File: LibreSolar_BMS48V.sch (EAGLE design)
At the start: 185 parts, among them IC1 BQ76940, Q1 ZXMP10A13F, Q10 DMN2004K, Q11 DMN2004K, Q12 DMN2004K, Q13 DMN2004K, Q14 DMN2004K, Q15 DMN2004K, Q16 DMN2004K, Q17 DMN2004K, Q18 DMN2004K, Q19 DMN2004K, Q2 FDMT80080DC, Q3 FDMT80080DC, Q4 2N7002ET1G, Q5 DMN2004K, Q6 DMN2004K, Q7 DMN2004K, Q8 DMN2004K, Q9 DMN2004K, U1 BQ76200, U2 LMR16006X, U3 ATMEGA328, Y1 8MHz

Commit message: Pinout of extension connector (LSX) changed
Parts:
- C10: value 4.7µ -> 1µ
- C11, C14, C16, C18: MF AVX -> MURATA; MPN 08053C105KAT2A -> GRM188R71E105KA12D; OC_FARNELL 1658877 -> 1735540
- C19: value 470n -> 1µ
- C20, C21: MF WALSIN -> MURATA; MPN 0603B104K500CT -> GRM188R71H103KA01D.; OC_FARNELL 2496834 -> 8819980
- C40: MF AVX -> WALSIN; MPN 08055C104KAT2A -> 0603B104K500CT
- D23, D24, D25, D26, H1, H2, H3, H4, JP4: OC_FARNELL (none) -> unknown
- L1: MF (none) -> COILCRAFT; MPN (none) -> LPS5030-104MLC
- LMX1: device resolut:LIBRE-STANDARD-EXTENSION -> LibreSolar:LIBRE-STD-EXT_SMALL
- Q1: MF (none) -> DIODES INC.; MPN (none) -> ZXMP10A13FTA; OC_FARNELL (none) -> 1843777
- R10: value 5m -> 1m
- R76: MF MULTICOMP -> PANASONIC ELECTRONIC COMPONENTS; MPN MCMR06X1001FTL -> ERJU06F1004V; OC_FARNELL 2073348 -> 2145441
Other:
- note added: "25V"
- note added: "Take resistor with low temperature coefficient and 3W thermal rating, e.g.: Bourns CRE2512-FZ-R001E-3 (75 ppm/K, 3W, 1%)"
- note added: "ToDo: - Mehrere Rsense parallel (package 2512 selbst bei 1 mOhm Widerstand nicht ausreichend für Verlustleistung)"
- note added: "Total gate capacitance of both FETs approx 40nF (see slva729a)"

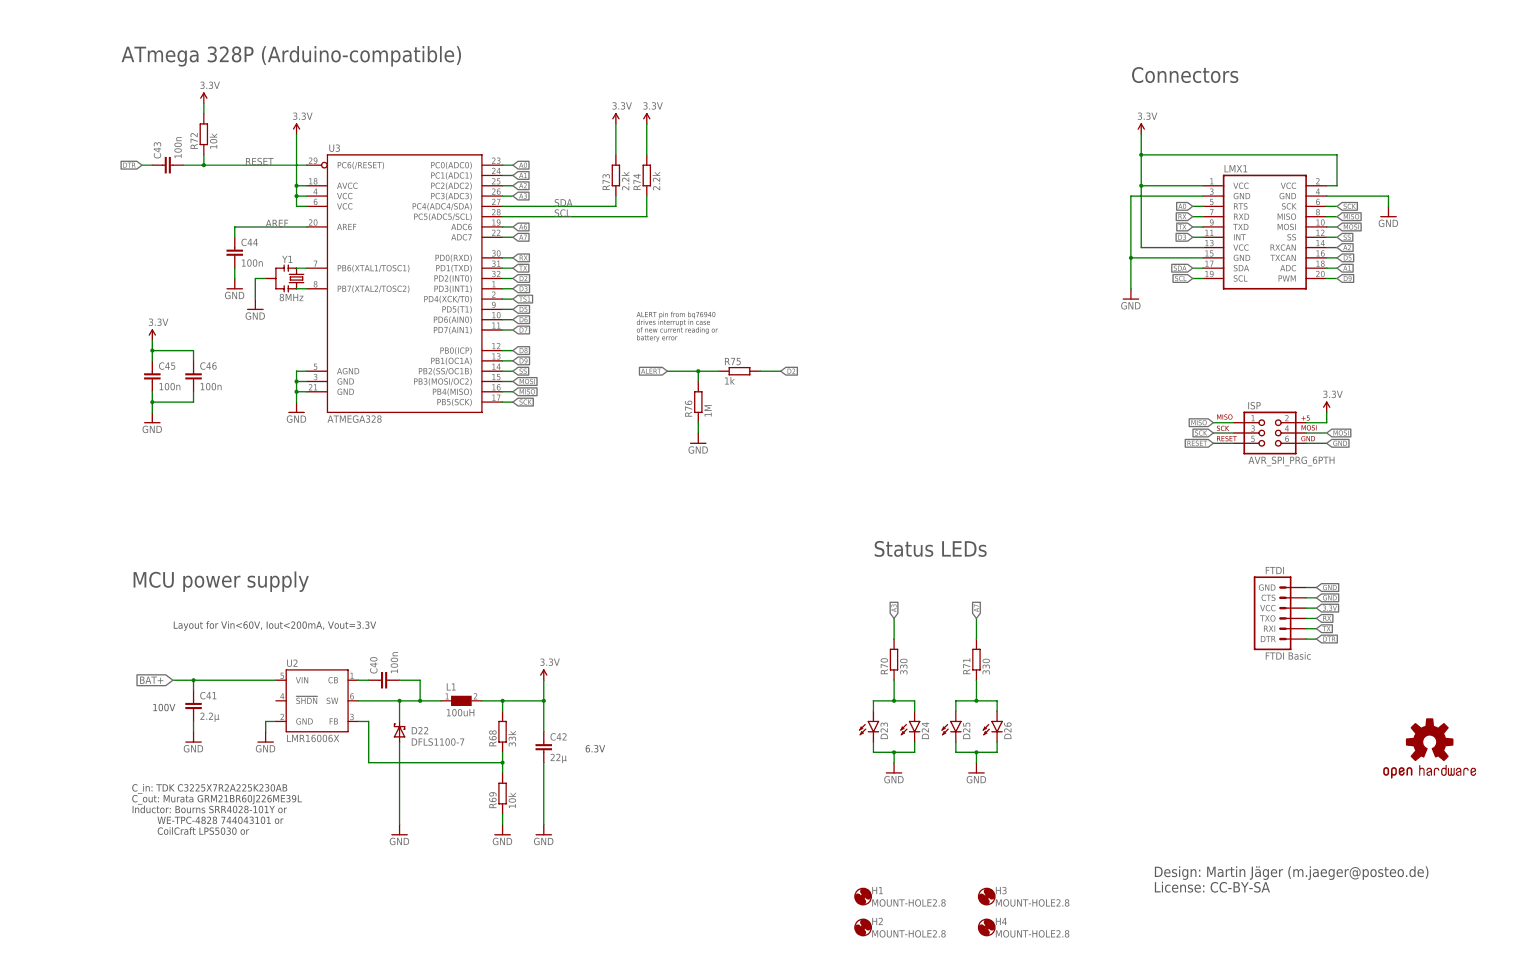
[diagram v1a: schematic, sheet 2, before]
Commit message: Complete redesign with STM32F072 and external power part
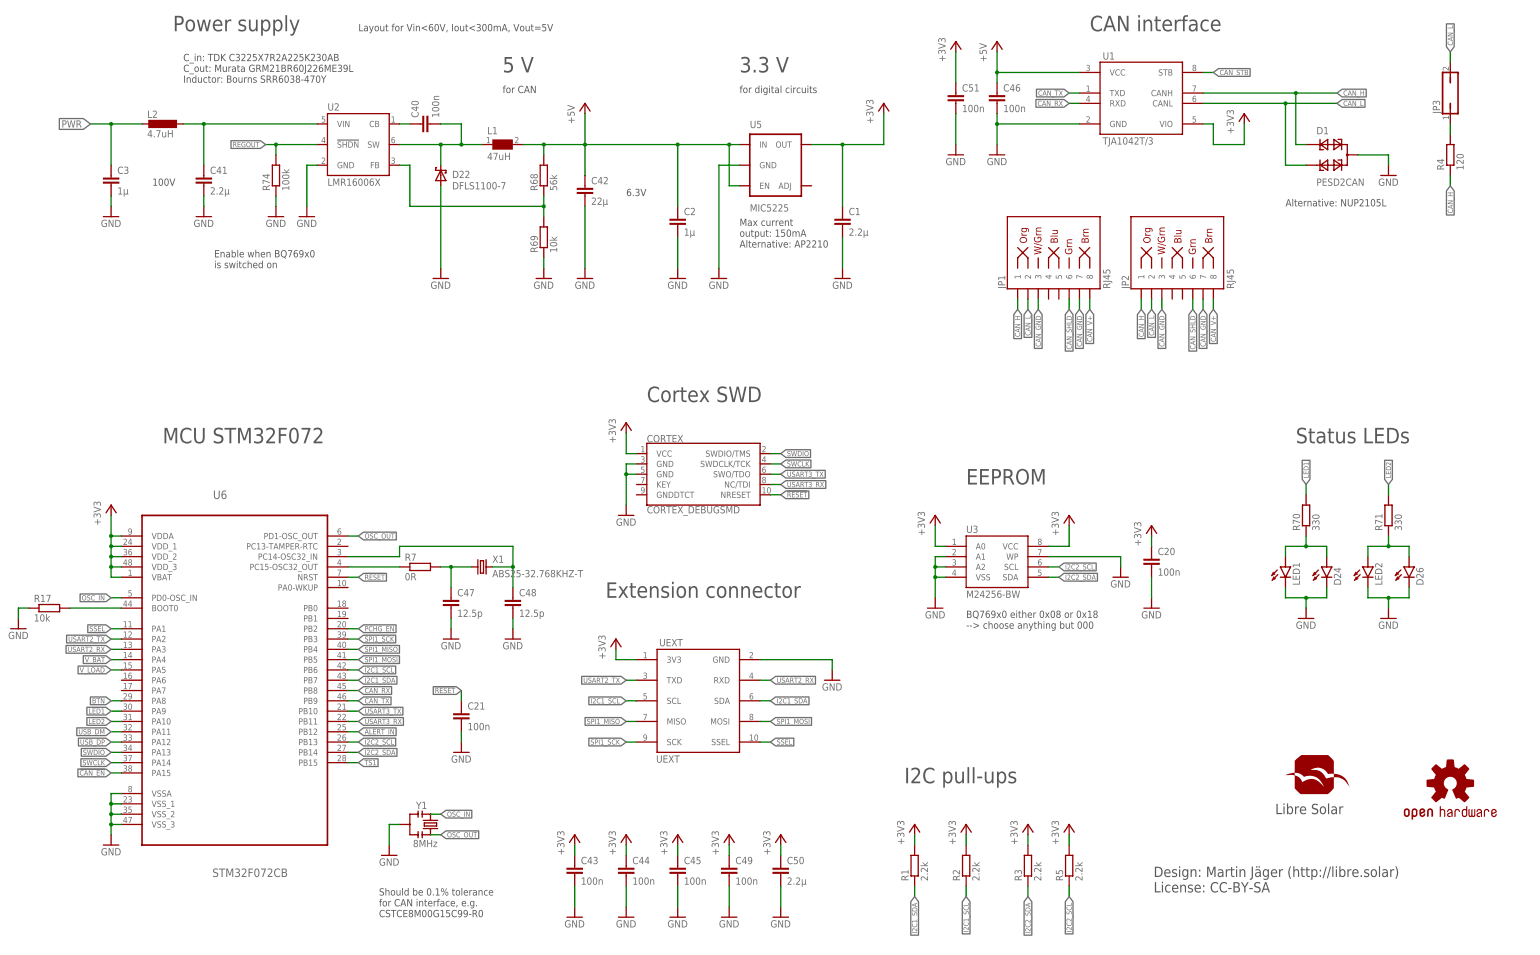
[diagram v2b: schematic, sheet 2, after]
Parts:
- removed BAT, LOAD: MKDS_5/2-9,52, resolut:MKDS_5/2-9,52
- removed D23, D25: (no value), SparkFun-LED:LED3MM
- removed FTDI: FTDI Basic, SparkFun:ARDUINO_SERIAL_PROGRAMPTH
- removed ISP: AVR_SPI_PRG_6PTH, SparkFun-Connectors:AVR_SPI_PRG_6PTH
- removed JP4: M02PTH, SparkFun-Connectors:M02PTH
- removed LMX1: (no value), LibreSolar:LIBRE-STD-EXT_SMALL
- removed Q1: ZXMP10A13F, SparkFun-DiscreteSemi:MOSFET-PCHANNEL
- removed Q2, Q3: FDMT80080DC, resolut:FDMT80080DC
- removed R10: 1m, rcl:R-EU_R2512
- removed R16: 100, rcl:R-EU_R0603
- removed R18: 100k, rcl:R-EU_R0603
- removed R19: 10k, rcl:R-EU_R0603
- removed SV1: (no value), con-lstb:MA10-2
- added C47, C48: 12.5p, rcl:C-EUC0603
- added C49, C51: 100n, rcl:C-EUC0603
- added C50: 2.2µ, rcl:C-EUC0603
- added CELLS: (no value), Wire_to_Board_Connectors_rev15d:66201821022
- added CORTEX: CORTEX_DEBUGSMD, LibreSolar:CORTEX_DEBUGSMD
- added D27, D28, D30: 3.3V, SparkFun-DiscreteSemi:DIODE-ZENER5.6V
- added D29: 1N4148W, SparkFun-DiscreteSemi:DIODESOD123
- added JP1, JP2: RJ45, SparkFun-Connectors:RJ45-8PTH
- added JP3: (no value), jumper:JP1Q
- added JP5: (no value), pinhead:PINHD-2X4
- added K1: 62000211622, Wire_to_Board_Connectors_rev15d:62000211622
- added K4: 66200621122, Wire_to_Board_Connectors_rev15d:66200621122
- added K5: 66201821122, Wire_to_Board_Connectors_rev15d:66201821122
- added L2: 4.7uH, rcl:L-EUL2012C
- added LED1, LED2: (no value), SparkFun-LED:LED3MM
- added R77, R79: 100k, rcl:R-EU_R0603
- added R78, R80: 5.6k, rcl:R-EU_R0603
- added S1: (no value), EAGLE-TACT_SWITCHES-rev16e:430182050816
- added TEMP: 66200621022, Wire_to_Board_Connectors_rev15d:66200621022
- added U$1: LIBRESOLAR_LOGO, LibreSolar:LIBRESOLAR_LOGO
- added U5: MIC5225, SparkFun-PowerIC:V_REG_MIC5235
- added U6: STM32F072CB, LibreSolar:STM32F072CB
- added UEXT: UEXT, LibreSolar:UEXT
- added X1: ABS25-32.768KHZ-T, crystal:CRYSTALMM20SS
- C1: value 100n -> 2.2µ; MF WALSIN -> AVX; MPN 0603B104K500CT -> 0805YC475KAT2A; OC_FARNELL 2496834 -> 1657937
- C10: device rcl:C-EUC0805 -> rcl:C-EUC0603
- C13, C15, C17: value 100n -> 4.7n
- C19: value 1µ -> 100n
- C2: value 100n -> 1µ; MF WALSIN -> AVX; MPN 0603B104K500CT -> 08055C104KAT2A; OC_FARNELL 2496834 -> 499687
- C20, C21: value 10n -> 100n; MPN GRM188R71H103KA01D. -> GRM188R71H104KA93D; OC_FARNELL 8819980 -> 8820023
- C3: value 100n -> 1µ; device rcl:C-EUC0603 -> rcl:C-EUC0805; MF WALSIN -> AVX; MPN 0603B104K500CT -> 08055C104KAT2A; OC_FARNELL 2496834 -> 499687
- C43, C44, C45: MF WALSIN -> MURATA; MPN 0603B104K500CT -> GRM188R71H104KA93D; OC_FARNELL 2496834 -> 8820023
- C46: MF WALSIN -> AVX; MPN 0603B104K500CT -> 06035C104KAT2A; OC_FARNELL 2496834 -> 1301804
- D1: value SMCJ75A -> PESD2CAN; device diode:SCHOTTKY-DIODESMC -> LibreSolar:PESD2CAN; MF FAIRCHILD SEMICONDUCTOR -> NXP; MPN SMCJ75A -> PESD2CAN; OC_FARNELL 2322496 -> 1510712
- D2: value ES3D-E3/57T -> 1N4148W; device diode:DIODE-SMC -> SparkFun-DiscreteSemi:DIODESOD123; MF VISHAY -> DIODES INC.; MPN ES3D-E3/57T. -> 1N4148W-7-F.; OC_FARNELL 1021753 -> 1776392
- D5: value 1N4148W -> 3.3V; device SparkFun-DiscreteSemi:DIODESOD123 -> SparkFun-DiscreteSemi:DIODE-ZENER5.6V; MF DIODES INC. -> NXP; MPN 1N4148W-7-F. -> BZX384-C5V6; OC_FARNELL 1776392 -> 8735743
- IC1: device resolut:BQ76940 -> LibreSolar:BQ76940
- L1: value 100uH -> 47uH; device PowerMagnetics:WE-TPC_4818/4828 -> PowerMagnetics:WE-TPC_6823; MF COILCRAFT -> (none); MPN LPS5030-104MLC -> (none); OC_FARNELL 2287830 -> (none)
- Q4: value 2N7002ET1G -> BSS123
- R1, R2, R5: value 33 -> 2.2k; device rcl:R-EU_R2010 -> rcl:R-EU_R0603; MF WELWYN -> YAGEO (PHYCOMP); MPN ASC2010-33RFT4 -> RC0603FR-072K2L.; OC_FARNELL 2079038 -> 9238522
- R15: value 100 -> 5.6k
- R17: value 100k -> 10k; MF (none) -> YAGEO (PHYCOMP); MPN (none) -> RC0603FR-0710KL; OC_FARNELL unknown -> 9238603
- R3: value 5 -> 2.2k; MF PANASONIC ELECTRONIC COMPONENTS -> YAGEO (PHYCOMP); MPN ERJU06F1004V -> RC0603FR-072K2L.; OC_FARNELL 2145441 -> 9238522
- R4: value 5 -> 120; device rcl:R-EU_R0603 -> rcl:R-EU_R1206; MF PANASONIC ELECTRONIC COMPONENTS -> WELWYN; MPN ERJU06F1004V -> WCR0805-120RFI; OC_FARNELL 2145441 -> 1100308
- R6: value 1M -> t.b.d.; MF PANASONIC ELECTRONIC COMPONENTS -> MULTICOMP; MPN ERJU06F1004V -> MCMR06X1001FTL; OC_FARNELL 2145441 -> 2073348
- R68: value 33k -> 56k
- R7: value 1M -> 0R; MF PANASONIC ELECTRONIC COMPONENTS -> YAGEO (PHYCOMP); MPN ERJU06F1004V -> RC0603FR-0710KL; OC_FARNELL 2145441 -> 9238603
- R72: value 10k -> 100k; MF PANASONIC ELECTRONIC COMPONENTS -> MULTICOMP; MPN ERJ3EKF1002V -> MCMR06X1001FTL; OC_FARNELL 2303192 -> 2073348
- R73: value 2.2k -> 10k
- R74: value 2.2k -> 100k; MF MULTICOMP -> PANASONIC ELECTRONIC COMPONENTS; MPN MCMR06X1001FTL -> ERJ3EKF1002V; OC_FARNELL 2073348 -> 2303192
- U1: value BQ76200 -> TJA1042T/3; device resolut:BQ76200 -> LibreSolar:TJA1042T/3; OC_FARNELL unknown -> (none)
- U3: value ATMEGA328 -> M24256-BW; device SparkFun:ATMEGA168 -> SparkFun-DigitalIC:EEPROM-I2CSMD; MF ATMEL -> (none); MPN ATMEGA328P-AUR -> (none); OC_FARNELL 2425124 -> (none)
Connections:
- removed net 3.3V: C42.1, C45.1, C46.1, FTDI.VCC, ISP.2, L1.2, LMX1.VCC@1, LMX1.VCC@2, LMX1.VCC@3, R68.2, R72.2, R73.2, R74.2, U3.AVCC, U3.VCC@1, U3.VCC@2
- removed net A0: LMX1.RTS, U3.PC0(ADC0)
- removed net A1: LMX1.ADC, U3.PC1(ADC1)
- removed net A2: LMX1.RXCAN, U3.PC2(ADC2)
- removed net A3: R70.2, U3.PC3(ADC3)
- removed net A6: R18.1, R19.2, U3.ADC6
- removed net A7: R71.2, U3.ADC7
- removed net AREF: C44.1, U3.AREF
- removed net CHG: R3.1, U1.CHG
- removed net CHGDSG: Q1.S, Q2.D, Q3.D
- removed net D2: R75.2, U3.PD2(INT0)
- removed net D3: LMX1.INT, U3.PD3(INT1)
- removed net D5: LMX1.TXCAN, U3.PD5(T1)
- removed net D6: U1.CP_EN, U3.PD6(AIN0)
- removed net D7: U1.PMON_EN, U3.PD7(AIN1)
- removed net D8: U1.PCHG_EN, U3.PB0(ICP)
- removed net D9: LMX1.PWM, U3.PB1(OC1A)
- removed net DSG: R4.1, U1.DSG
- removed net DTR: C43.1, FTDI.DTR
- removed net MISO: ISP.1, LMX1.MISO, U3.PB4(MISO)
- removed net MOSI: ISP.4, LMX1.MOSI, U3.PB3(MOSI/OC2)
- removed net N$26: C3.2, C7.1
- removed net N$38: C19.2, U1.VDDCP
- removed net N$47: C8.1, D3.C, IC1.BAT, R11.1
- removed net N$48: C1.2, C2.1
- removed net N$50: Q2.G, R3.2, R6.1
- removed net N$52: Q1.D, R1.1
- removed net N$54: R2.2, R5.2
- removed net N$55: R1.2, R2.1
- removed net N$6: Q3.G, R4.2, R7.1
- removed net PACK+: C2.2, C3.1, D2.C, LOAD-2.KL, Q3.S, R16.2, R5.1, R7.2
- removed net PACK-: C7.2, D2.A, LOAD-1.KL, R10.2, R9.1
- removed net PCHG: Q1.G, U1.PCHG
- removed net RESET: C43.2, ISP.5, R72.1, U3.PC6(/RESET)
- removed net RX: FTDI.TXO, LMX1.RXD, U3.PD0(RXD)
- removed net SCK: ISP.3, LMX1.SCK, U3.PB5(SCK)
- removed net SCL: IC1.SCL, LMX1.SCL, R74.1, U3.PC5(ADC5/SCL)
- removed net SDA: IC1.SDA, LMX1.SDA, R73.1, U3.PC4(ADC4/SDA)
- removed net SS: LMX1.SS, U3.PB2(SS/OC1B)
- removed net TX: FTDI.RXI, LMX1.TXD, U3.PD1(TXD)
- new net !CAN_EN!: U6.PA15
- new net !RESET: C21.1, CORTEX.NRESET, U6.NRST
- new net +3V3: C1.1, C20.1, C43.1, C44.1, C45.1, C49.1, C50.1, C51.1, CORTEX.VCC, R1.2, R2.2, R3.2, R5.2, U1.VIO, U3.A0, U3.VCC, U5.OUT, U6.VBAT, U6.VDDA, U6.VDD_1, U6.VDD_2, U6.VDD_3, UEXT.3V3
- new net +5V: C2.1, C42.1, C46.1, L1.2, R68.2, U1.VCC, U5.EN, U5.IN
- new net ALERT_IN: R75.2, U6.PB12
- new net BAT: C8.1, D4.C, IC1.BAT, R11.2
- new net BAT-: JP5.5
- new net BTN: D30.C, R72.2, R73.1, U6.PA8
- new net CAN_GND: JP1.3, JP1.7, JP2.3, JP2.7
- new net CAN_H: D1.1, JP1.1, JP2.1, R4.1, U1.CANH
- new net CAN_L: D1.2, JP1.2, JP2.2, JP3.2, U1.CANL
- new net CAN_RX: U1.RXD, U6.PB8
- new net CAN_SHLD: JP1.6, JP2.6
- new net CAN_STB: U1.STB
- new net CAN_TX: U1.TXD, U6.PB9
- new net CAN_V+: JP1.8, JP2.8
- new net I2C1_SCL: R2.1, U6.PB6, UEXT.SCL
- new net I2C1_SDA: R1.1, U6.PB7, UEXT.SDA
- new net I2C2_SCL: IC1.SCL, R5.1, U3.SCL, U6.PB13
- new net I2C2_SDA: IC1.SDA, R3.1, U3.SDA, U6.PB14
- new net LED1: R70.2, U6.PA9
- new net LED2: R71.2, U6.PA10
- new net LOAD+: JP5.3, R79.2
- new net MCU_IN: D29.A, K1.1, R73.2, S1.2, S1.4
- new net N$57: R17.2, U6.BOOT0
- new net OSC_IN: U6.PD0-OSC_IN, Y1.1
- new net OSC_OUT: U6.PD1-OSC_OUT, Y1.3
- new net PCHG_EN: JP5.6, U6.PB2
- new net PWR: C3.1, CELLS.18, D6.A, K5.18, L2.2, R11.1, R6.1, R77.2
- new net R_SENSE+: JP5.7, R8.1
- new net R_SENSE-: JP5.8, R9.1
- new net SPI1_MISO: U6.PB4, UEXT.MISO
- new net SPI1_MOSI: U6.PB5, UEXT.MOSI
- new net SPI1_SCK: U6.PB3, UEXT.SCK
- new net SSEL: U6.PA1, UEXT.SSEL
- new net SWCLK: CORTEX.SWDCLK/TCK, U6.PA14
- new net SWDIO: CORTEX.SWDIO/TMS, U6.PA13
- new net USART2_RX: U6.PA3, UEXT.RXD
- new net USART2_TX: U6.PA2, UEXT.TXD
- new net USART3_RX: CORTEX.NC/TDI, U6.PB11
- new net USART3_TX: CORTEX.SWO/TDO, U6.PB10
- new net USB_DM: U6.PA11
- new net USB_DP: U6.PA12
- new net V_BAT: C19.1, R77.1, R78.2, U6.PA4
- new net V_LOAD: C7.1, R79.1, R80.2, U6.PA5
- net BAT+: now also JP5.1; no longer BAT-1.KL, C1.1, C41.1, D1.C, D6.A, Q2.S, R11.2, R15.2, R6.2, U2.VIN
- net C0: now also CELLS.10, K5.10; no longer SV1.1
- net C1: now also CELLS.2, K5.2; no longer SV1.2
- net C10: now also CELLS.15, K5.15; no longer SV1.11
- net C11: now also CELLS.7, K5.7; no longer SV1.12
- net C12: now also CELLS.16, K5.16; no longer SV1.13
- net C13: now also CELLS.8, K5.8; no longer SV1.14
- net C14: now also CELLS.17, K5.17; no longer SV1.15
- net C15: now also CELLS.9, K5.9; no longer SV1.16
- net C2: now also CELLS.11, K5.11; no longer SV1.3
- net C3: now also CELLS.3, K5.3; no longer SV1.4
- net C4: now also CELLS.12, K5.12; no longer SV1.5
- net C5: now also CELLS.4, K5.4; no longer SV1.6
- net C6: now also CELLS.13, K5.13; no longer SV1.7
- net C7: now also CELLS.5, K5.5; no longer SV1.8
- net C8: now also CELLS.14, K5.14; no longer SV1.9
- net C9: now also CELLS.6, K5.6; no longer SV1.10
- net CAP2: now also IC1.NC11, IC1.NC12
- net CAP3: now also IC1.NC16, IC1.NC17
- net CHG_EN: now also JP5.2; no longer U1.CHG_EN
- net DSG_EN: now also JP5.4; no longer U1.DSG_EN
- net GND: now also C1.2, C19.2, C2.2, C3.2, C37.2, C43.2, C47.2, C48.2, C49.2, C50.2, C51.2, C7.2, CELLS.1, CORTEX.GND@3, CORTEX.GND@5, D1.3, D27.A, D28.A, D30.A, D5.A, K4.1, K5.1, LED1.C, LED2.C, R17.1, R72.1, R74.1, R78.1, R80.1, TEMP.1, U1.GND, U3.A1, U3.A2, U3.VSS, U3.WP, U5.GND, U6.VSSA, U6.VSS_1, U6.VSS_2, U6.VSS_3, UEXT.GND; no longer BAT-2.KL, C37.1, D1.A, D23.C, D25.C, FTDI.CTS, FTDI.GND, ISP.6, LMX1.GND@1, LMX1.GND@2, LMX1.GND@3, R10.1, R19.1, R8.1, SV1.17, U1.VSS, U3.AGND, U3.GND@1, U3.GND@2
- net N$10: now also D29.C, R15.2; no longer U3.PB6(XTAL1/TOSC1), Y1.1
- net N$40: now also JP3.1, R4.2; no longer C19.1, C20.1, R15.1, U1.BAT
- net N$41: now also R7.1, U6.PC15-OSC32_OUT; no longer C21.1, R16.1, U1.PACK
- net N$42: now also C47.1, R7.2, X1.1; no longer R17.2, U1.PACKDIV
- net N$43: now also LED1.A; no longer D23.A
- net N$44: now also C48.1, U6.PC14-OSC32_IN, X1.2; no longer R17.1, R18.2
- net N$46: now also LED2.A; no longer D25.A
- net N$49: now also R6.2
- net N$9: now also C41.1, L2.1, U2.VIN; no longer U3.PB7(XTAL2/TOSC2), Y1.3
- net REGOUT: now also R74.2, U2.!SHDN!
- net SRN: now also D28.C
- net SRP: now also D27.C
- net TS1: now also K4.4, R15.1, TEMP.4, U6.PB15; no longer SV1.18, U3.PD4(XCK/T0)
- net TS2: now also K4.5, TEMP.5; no longer SV1.20
- net TS3: now also K4.6, TEMP.6; no longer JP4.2
- net VC0: now also C37.1, D5.C; no longer C37.2
- net VC1: now also K1.2, S1.1, S1.3
- net VC10: now also D3.A; no longer D4.A
- net VC10X: now also D3.C, K4.3, TEMP.3; no longer D4.C, JP4.1
- net VC15: now also D4.A; no longer D3.A
- net VC5: now also D2.A; no longer D5.A
- net VC5X: now also D2.C, K4.2, TEMP.2; no longer D5.C, SV1.19
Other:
- note added: "2-5V"
- note added: "3.3 V"
- note added: "3V3 Zener: MM3Z3V3T1G"
- note added: "5 V"
- note added: "Alternative: NUP2105L"
- note added: "BAT+ and BAT- unused, power supply via cell connector to prevent damages due to wrong connection order"
- note added: "BQ769x0 either 0x08 or 0x18 --> choose anything but 000"
- note added: "Balancing (33R resistors) Current: 100-130 mA (3.3V-4.2V) Heat dissipation: 300-600 mW Zener diode 5.6V: BZX384-C5V6 or MM3Z5V6T1G or MMSZ5232BS-7-F"
- note added: "Boot switch"
- note added: "CAN interface"
- note added: "C_in: TDK C3225X7R2A225K230AB C_out: Murata GRM21BR60J226ME39L Inductor: Bourns SRR6038-470Y"
- note added: "Cortex SWD"
- note added: "Design: Martin Jäger (http://libre.solar) License: CC-BY-SA"
- note added: "EEPROM"
- note added: "Enable when BQ769x0 is switched on"
- note added: "Extension connector"
- note added: "For bq76930: Short C8, don't put TS3, C17, C18, R12"
- note added: "I2C pull-ups"
- note added: "JST PH compatible"
- note added: "Layout for Vin<60V, Iout<300mA, Vout=5V"
- note added: "MCU STM32F072"
- note added: "Max current output: 150mA Alternative: AP2210"
- note added: "Power supply"
- note added: "Protect VC5 from rising faster than VC5X"
- note added: "Should be 0.1% tolerance for CAN interface, e.g. CSTCE8M00G15C99-R0"
- note added: "Source follower for decreased voltage drop in internal LDO (100V N-MOS)"
- note added: "for CAN"
- note added: "for digital circuits"
- note removed: "ATmega 328P (Arduino-compatible)"
- note removed: "Balancing (33R resistors) Current: 100-130 mA (3.3V-4.2V) Heat dissipation: 300-600 mW"
- note removed: "C_in: TDK C3225X7R2A225K230AB C_out: Murata GRM21BR60J226ME39L Inductor: Bourns SRR4028-101Y or WE-TPC-4828 744043101 or CoilCraft LPS5030 or"
- note removed: "Chg/Dsg FETs"
- note removed: "Connectors"
- note removed: "Design: Martin Jäger (m.jaeger@posteo.de) License: CC-BY-SA"
- note removed: "FET driver"
- note removed: "Layout for Vin<60V, Iout<200mA, Vout=3.3V"
- note removed: "MCU power supply"
- note removed: "Purpose not clear... See reference design"
- note removed: "Switchable voltage divider: PACKDIV current max. 500 uA Pack voltage max. 60V + transients uC pin voltage = 60V * 10/210 = 2.86V"
- note removed: "Take resistor with low temperature coefficient and 3W thermal rating, e.g.: Bourns CRE2512-FZ-R001E-3 (75 ppm/K, 3W, 1%)"
- note removed: "ToDo: - Mehrere Rsense parallel (package 2512 selbst bei 1 mOhm Widerstand nicht ausreichend für Verlustleistung)"
- note removed: "Total gate capacitance of both FETs approx 40nF (see slva729a)"
- moved on the sheet: C10, C11, C12, C13, C14, C15, C16, C17, C18, C19, C22, C37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

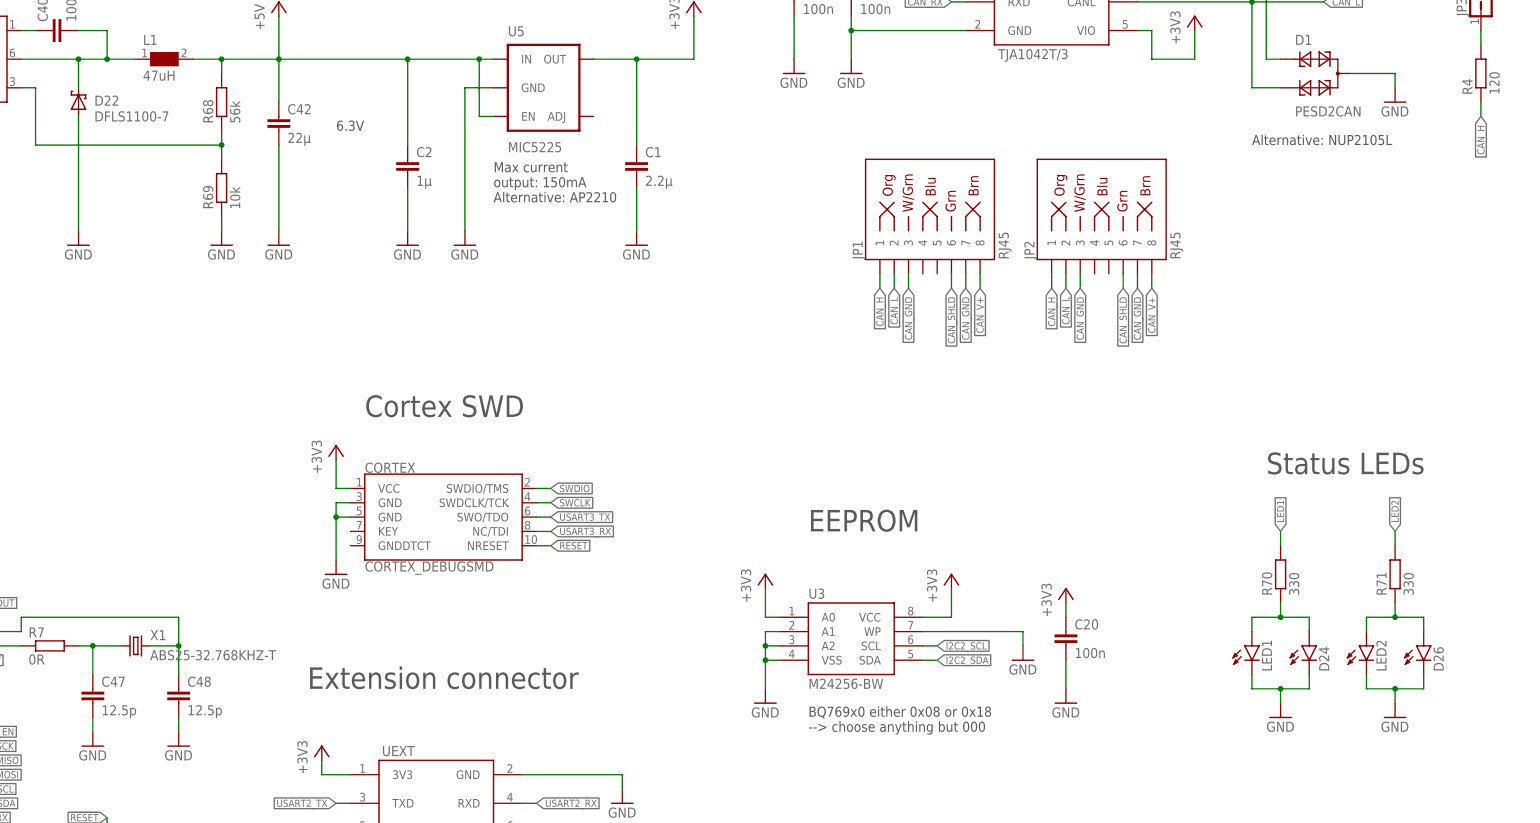
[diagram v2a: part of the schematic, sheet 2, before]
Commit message: Uploaded image of assembled PCB
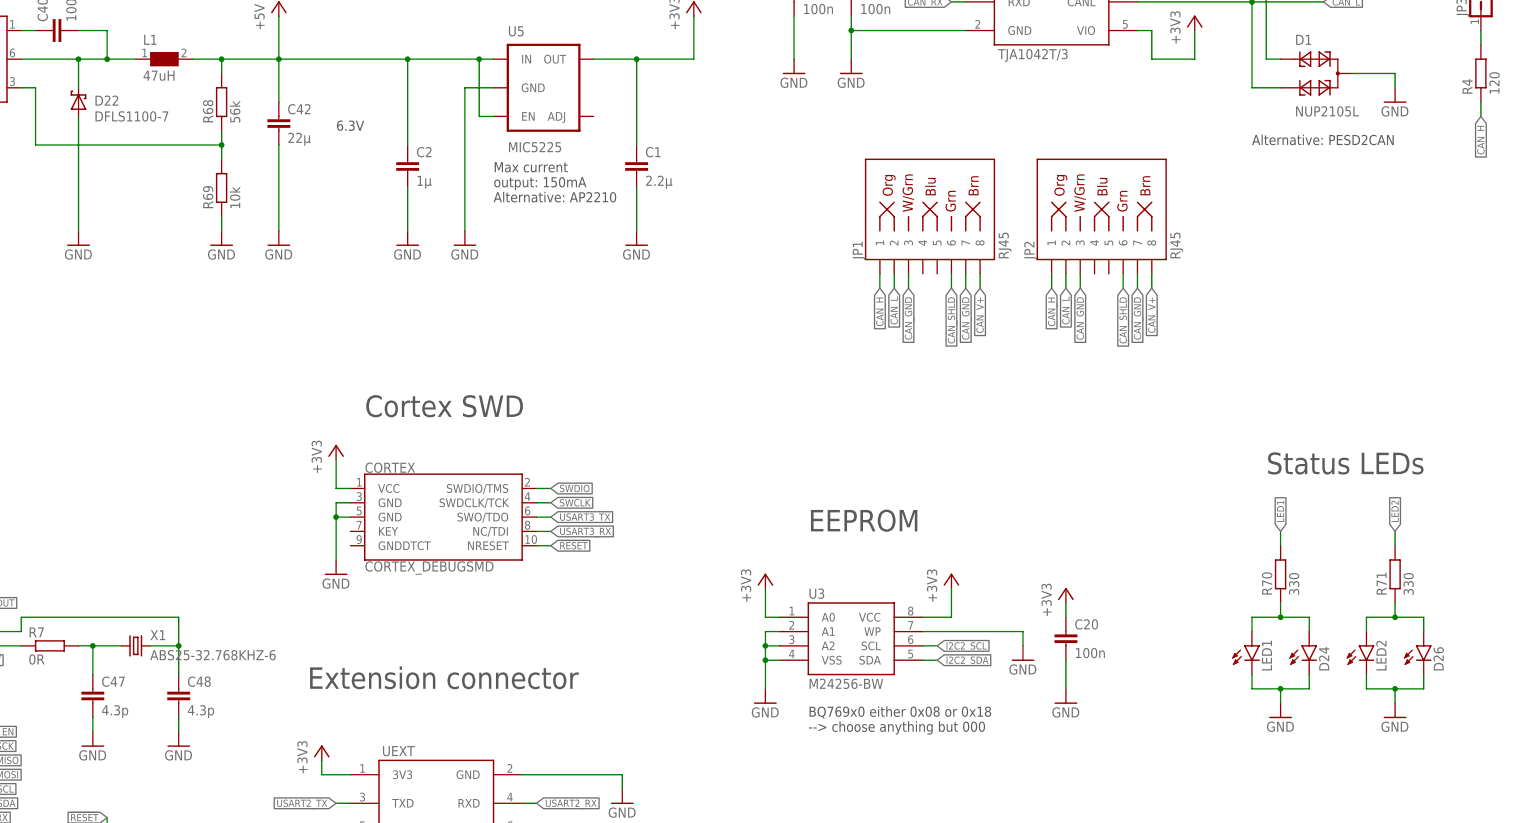
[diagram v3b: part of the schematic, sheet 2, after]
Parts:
- C47, C48: value 12.5p -> 4.3p
- D1: value PESD2CAN -> NUP2105L
- X1: value ABS25-32.768KHZ-T -> ABS25-32.768KHZ-6
- Y1: MPN CSTCE8M00G55-R0 -> CSTCE8M00G15C99-R0; OC_FARNELL 2443270 -> (none)
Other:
- note added: "Alternative: PESD2CAN"
- note removed: "Alternative: NUP2105L"
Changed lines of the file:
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@@
 <?xml version="1.0" encoding="utf-8"?>
 <!DOCTYPE eagle SYSTEM "eagle.dtd">
-<eagle version="7.6.0">
+<eagle version="7.7.0">
 <drawing>
 <settings>
@@
 <attribute name="OC_FARNELL" value="1100308"/>
 </part>
-<part name="D1" library="LibreSolar" deviceset="PESD2CAN" device="" value="PESD2CAN">
+<part name="D1" library="LibreSolar" deviceset="PESD2CAN" device="" value="NUP2105L">
 <attribute name="MF" value="NXP"/>
 <attribute name="MPN" value="PESD2CAN"/>
@@
 <part name="GND40" library="SparkFun-Aesthetics" deviceset="GND" device=""/>
 <part name="CORTEX" library="LibreSolar" deviceset="CORTEX_DEBUG" device="SMD"/>
-<part name="X1" library="crystal" deviceset="CRYSTAL" device="MM20SS" value="ABS25-32.768KHZ-T"/>
-<part name="C47" library="rcl" deviceset="C-EU" device="C0603" value="12.5p">
+<part name="X1" library="crystal" deviceset="CRYSTAL" device="MM20SS" value="ABS25-32.768KHZ-6"/>
+<part name="C47" library="rcl" deviceset="C-EU" device="C0603" value="4.3p">
 <attribute name="MF" value="MURATA"/>
 <attribute name="MPN" value="GRM188R71H104KA93D"/>
 <attribute name="OC_FARNELL" value="8820023"/>
 </part>
-<part name="C48" library="rcl" deviceset="C-EU" device="C0603" value="12.5p">
+<part name="C48" library="rcl" deviceset="C-EU" device="C0603" value="4.3p">
 <attribute name="MF" value="MURATA"/>
 <attribute name="MPN" value="GRM188R71H104KA93D"/>
@@
 <part name="Y1" library="Testing" deviceset="RESONATOR" device="1:1" value="8MHz">
 <attribute name="MF" value="MURATA"/>
-<attribute name="MPN" value="CSTCE8M00G55-R0"/>
-<attribute name="OC_FARNELL" value="2443270"/>
+<attribute name="MPN" value="CSTCE8M00G15C99-R0"/>
 </part>
 <part name="GND3" library="supply1" deviceset="GND" device=""/>
@@
 <text x="274.32" y="238.76" size="3.81" layer="97">CAN interface</text>
 <text x="228.6" y="53.34" size="3.81" layer="97">I2C pull-ups</text>
-<text x="322.58" y="195.58" size="1.778" layer="97">Alternative: NUP2105L</text>
+<text x="322.58" y="195.58" size="1.778" layer="97">Alternative: PESD2CAN</text>
 <text x="99.06" y="20.32" size="1.778" layer="97">Should be 0.1% tolerance
 for CAN interface, e.g.
@@
 <attribute name="NAME" x="108.204" y="46.99" size="1.778" layer="95"/>
 <attribute name="VALUE" x="107.442" y="37.592" size="1.778" layer="96"/>
-<attribute name="OC_FARNELL" x="111.76" y="43.18" size="1.27" layer="96" display="off"/>
 <attribute name="MF" x="111.76" y="43.18" size="1.27" layer="96" display="off"/>
 <attribute name="MPN" x="111.76" y="43.18" size="1.27" layer="96" display="off"/>
